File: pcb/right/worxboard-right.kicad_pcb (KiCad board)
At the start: 2 copper layers, 182.8 x 158.8 mm, 141 parts, among them J1 TYPE-C-31-M-12, J2 PJ-320D-4A, J3 nice!view, SW1 BOOT, SW2 RESET, U1 RP2040, U2 W25Q128JVSIQ, U3 AP2112K-3.3, U4 USBLC6-2SC6, U5 USBLC6-2SC6, Y1 12MHz

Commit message: feat(pcb): route both halves to 0 unconnected (DRC + checks pass)
- negotiate: protected nets are dear rather than fixed, GND judged on a fresh fill,
  stuck nets spared on the next try, lanes kept clear ahead of locked stub ends
- pours join pads by overlap and tracks / vias only by anchor, as in KiCad
- left and right boards regenerated: 0 violations, 0 unconnected, 0 parity issues
- deviations WS2b-6 (rip-up) and WS2b-7 (left U4 keepout gap)

Co-Authored-By: Claude Opus 5.5 <noreply@anthropic.com>
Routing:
- net ROW5: track 120.3 -> 271.1 mm, vias 6 -> 16
- net DISP_SCK: track 3.09 -> 101.7 mm, vias 0 -> 3
- net DISP_MOSI: track 3.39 -> 97.4 mm, vias 0 -> 1
- net DISP_DC: track 6.65 -> 84.1 mm, vias 1 -> 2
- net ROW1: track 137.9 -> 190.4 mm, vias 7 -> 10
- net COL0: track 115.2 -> 165.8 mm, vias 6 -> 8
- net COL3: track 237.2 -> 278.4 mm, vias 11 -> 16
- net COL2: track 188.1 -> 228.2 mm, vias 7 -> 12
- net TRRS_DET: track 21.0 -> 40.1 mm, vias 2 -> 4
- net COL1: track 194.6 -> 212.3 mm, vias 8 -> 12
- net UART_RX: track 111.3 -> 128.6 mm, vias 4 -> 9
- net QSPI_SD1: track 5.33 -> 22.3 mm
- net QSPI_SD2: track 2.49 -> 19.0 mm, vias 0 -> 1
- net 1V1: track 46.0 -> 29.4 mm, vias 8 -> 4
- net VLINK: track 183.0 -> 168.8 mm
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
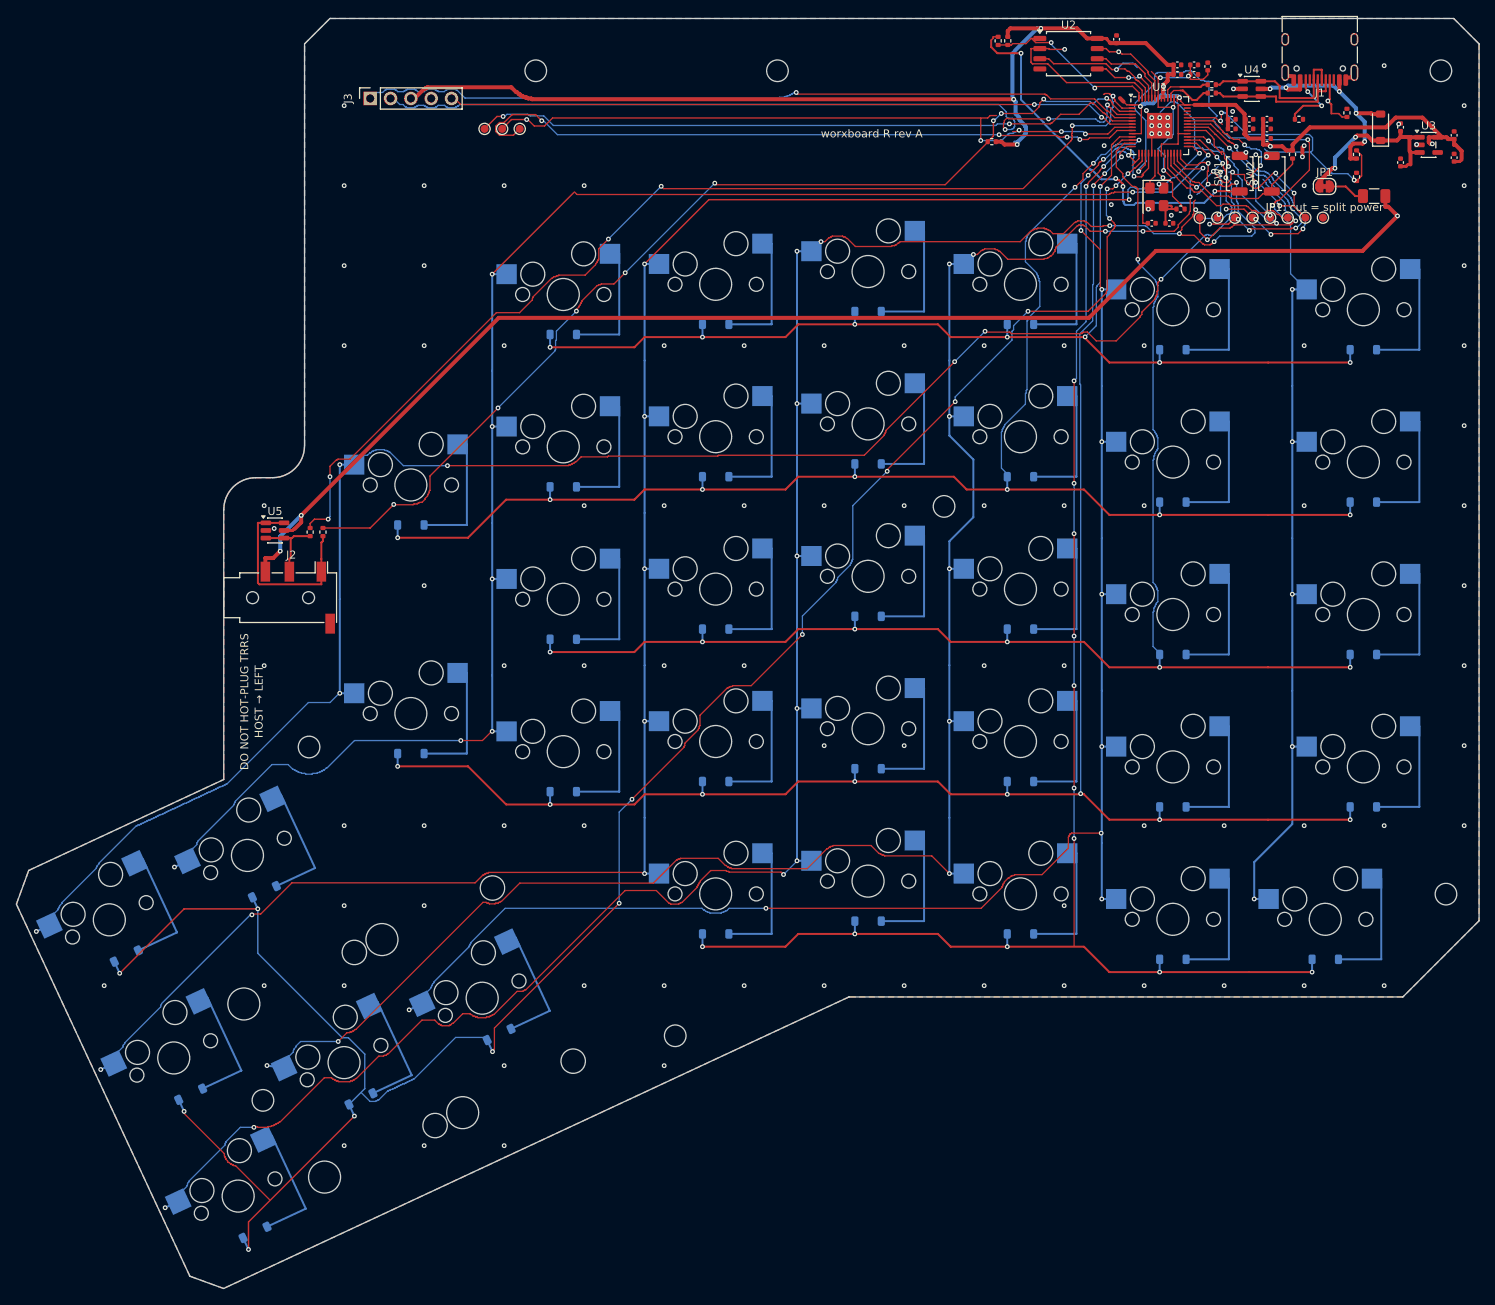
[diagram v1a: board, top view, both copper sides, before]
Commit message: feat(pcb): seed KIIDs and the hash seed so a clean rebuild reproduces the boards
place/route_critical/import_ses seed KiCad's UUID generator from their inputs and a
per-side base seed; pcb.just runs with PYTHONHASHSEED=0. Boards re-made from scratch
with the seeded pipeline (DRC 0 violations, 0 unconnected, checks pass), renders refreshed.

Co-Authored-By: Claude Opus 5.5 <noreply@anthropic.com>
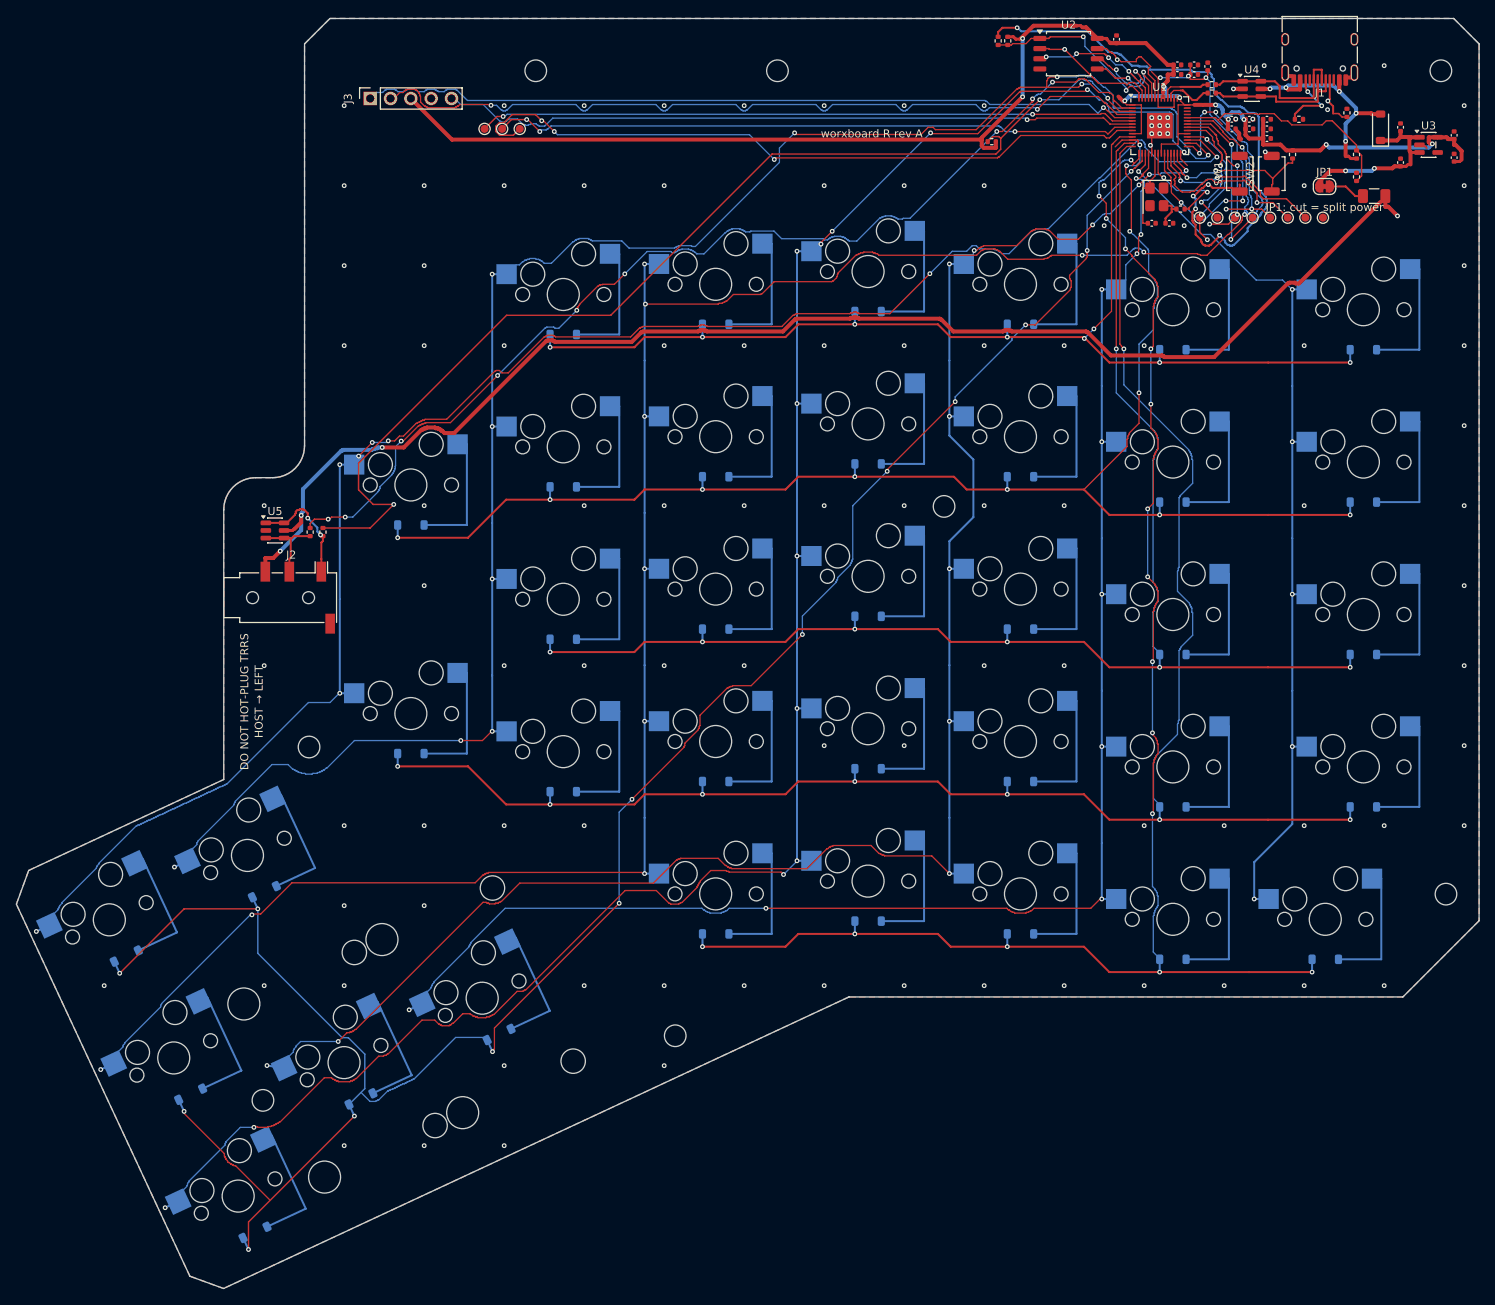
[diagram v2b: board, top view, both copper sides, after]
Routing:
- net COL0: track 165.8 -> 114.6 mm, vias 8 -> 6
- net COL4: track 239.8 -> 278.4 mm, vias 9 -> 14
- net COL3: track 278.4 -> 245.5 mm, vias 16 -> 13
- net BOOT: track 46.8 -> 74.7 mm, vias 4 -> 5
- net TRRS_DET: track 40.1 -> 18.3 mm, vias 4 -> 3
- net 1V1: track 29.4 -> 50.5 mm, vias 4 -> 6
- net COL5: track 209.5 -> 226.5 mm, vias 8 -> 10
- net COL1: track 212.3 -> 196.1 mm, vias 12 -> 10
- net TP5: track 32.4 -> 19.0 mm, vias 5 -> 3
- net TRRS_A: track 24.9 -> 13.6 mm, vias 0 -> 2
- net UART_RX: track 128.6 -> 139.7 mm, vias 9 -> 3
- net SWDIO: track 33.2 -> 22.9 mm, vias 6 -> 2
- net TP6: track 32.4 -> 22.4 mm, vias 5 -> 2
- net 3V3: track 205.6 -> 197.6 mm, vias 8 -> 10
- net VBUS_SENSE: track 37.5 -> 29.6 mm, vias 3 -> 0
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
